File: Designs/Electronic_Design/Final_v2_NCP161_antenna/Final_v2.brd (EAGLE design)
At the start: 134.7 x 20.4 mm, 5 parts

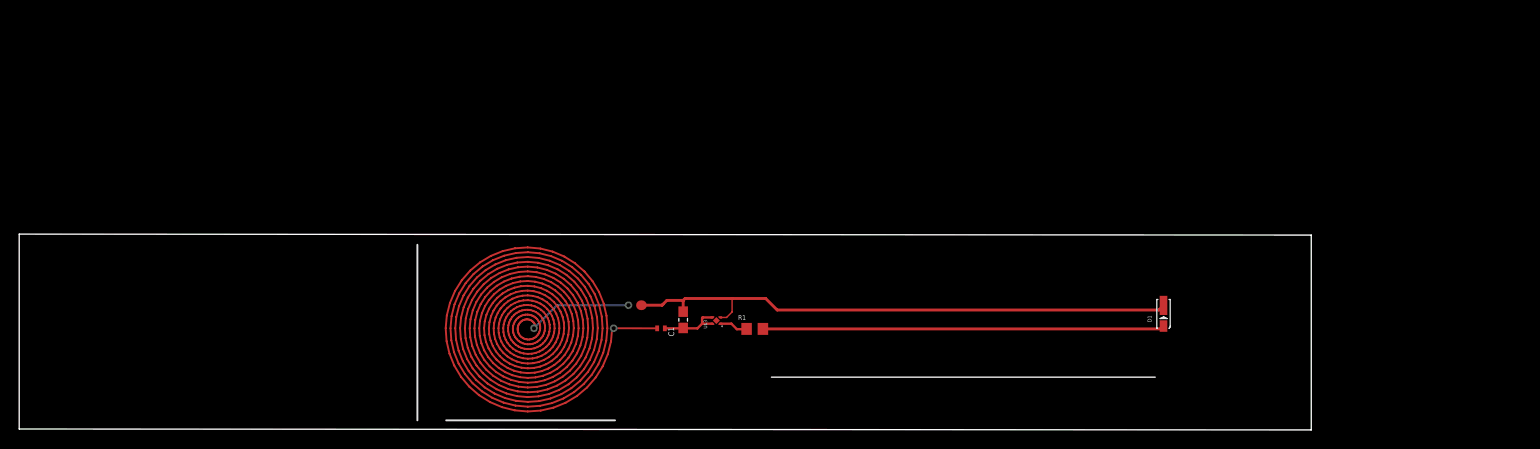
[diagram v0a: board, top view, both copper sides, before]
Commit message: NFC Charging
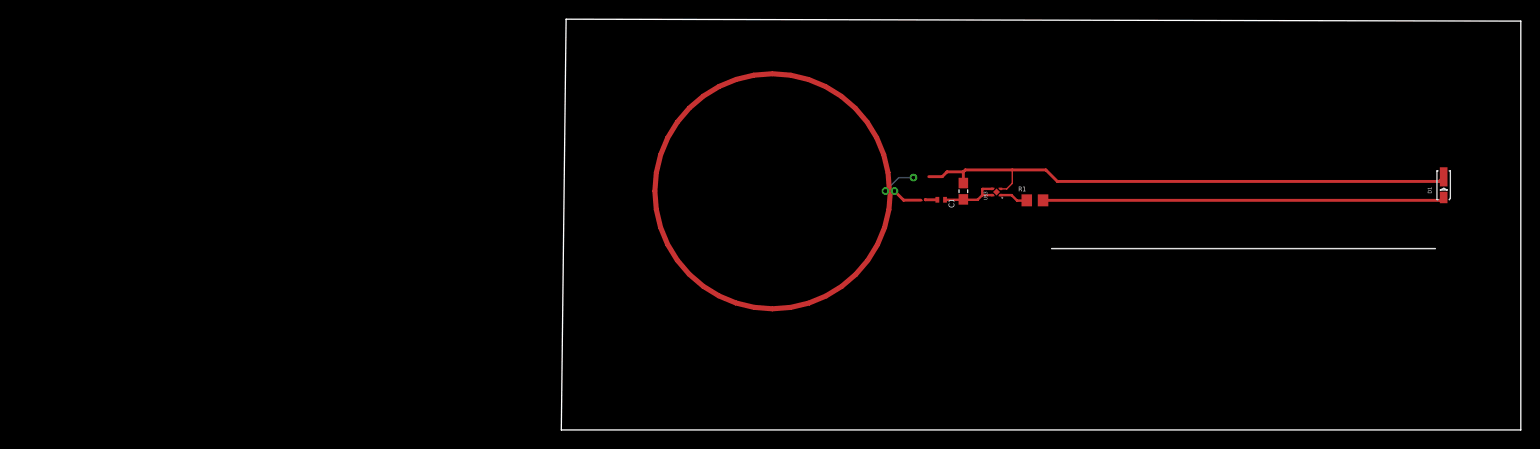
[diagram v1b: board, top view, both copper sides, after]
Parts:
- moved U$2 32.1 mm to (39.6, 24.0)
- moved C1 32.1 mm to (41.9, 24.9)
- moved D1 32.1 mm to (92.0, 25.5)
- moved R1 32.1 mm to (49.4, 23.9)
- moved U$3 32.1 mm to (45.4, 24.8)
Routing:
- net IN+: track 497.8 -> 1.26 mm, vias 3 -> 0
- net N$1: track 0.00 -> 391.6 mm, vias 0 -> 3
- net GND: track 59.6 -> 58.8 mm
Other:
- board size 134.7 x 20.4 mm -> 100 x 42.8 mm
